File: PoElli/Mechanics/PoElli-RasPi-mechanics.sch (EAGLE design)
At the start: 30 parts, among them J1 DF12-ELLI-HEADER-TOP, J3 M022.54MM, J4 M022.54MM, T1 Coilcraft 230NL, T2 FLYBACK750311689, U3 FST3257, X1 M-BOLT-2, X2 M-BOLT-2, X3 M-BOLT-2, X4 M-BOLT-2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

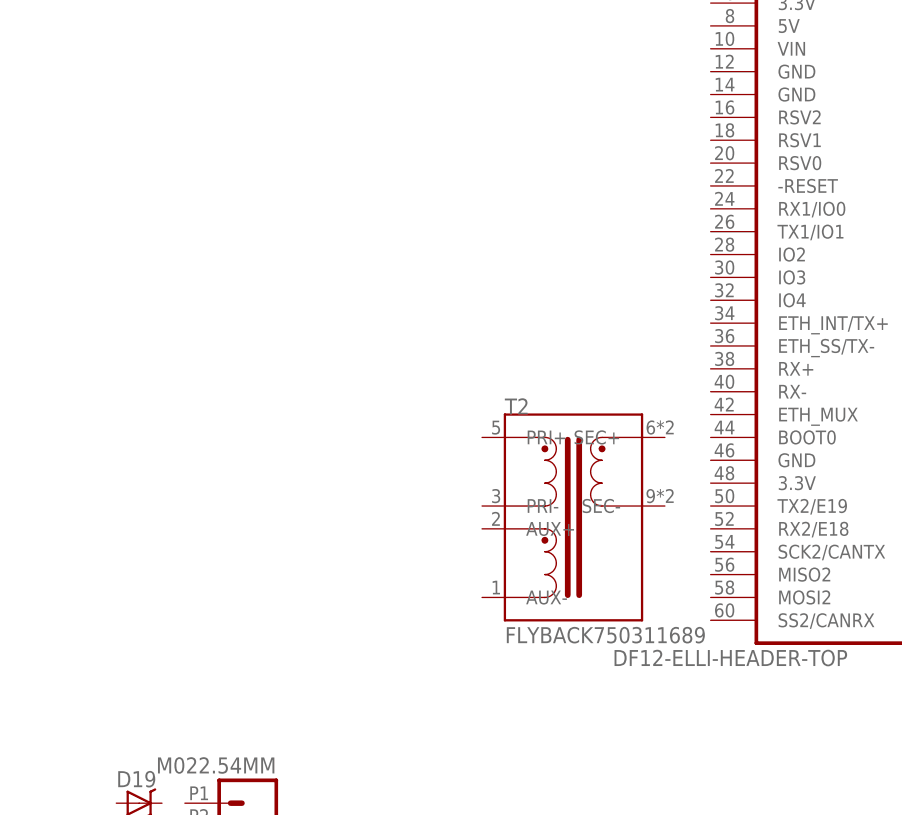
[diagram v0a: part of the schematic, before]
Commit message: Update PoElli/Mechanics non-produced boards with new library components
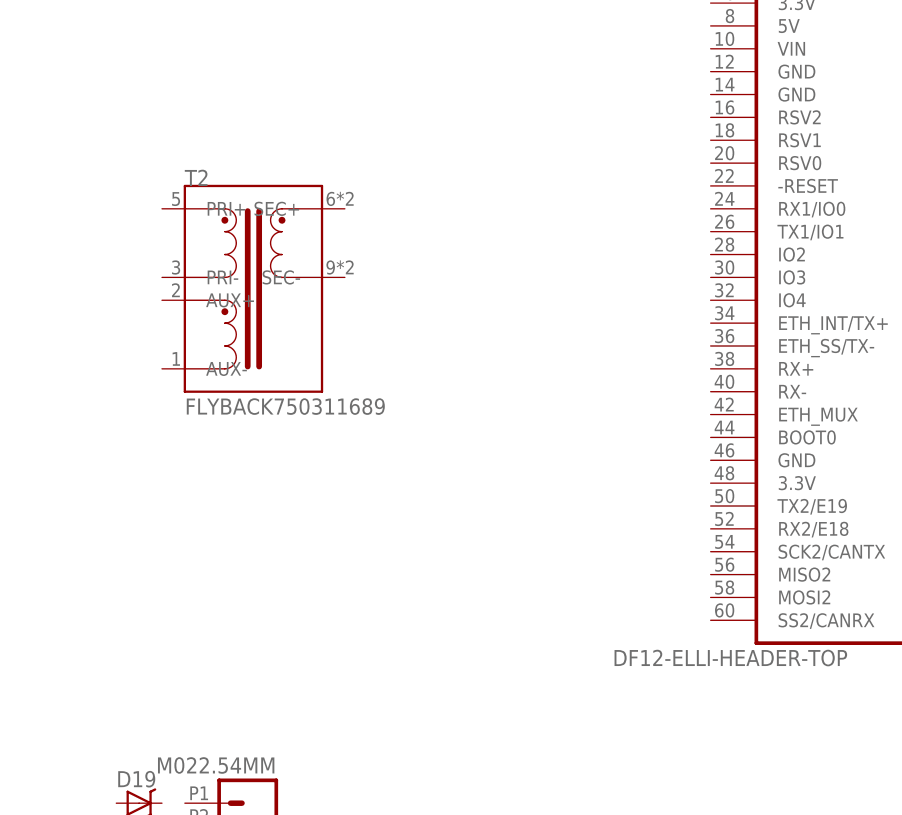
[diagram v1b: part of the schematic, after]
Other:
- moved on the sheet: T2
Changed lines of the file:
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@@
 <grid distance="0.1" unitdist="inch" unit="inch" style="lines" multiple="1" display="no" altdistance="0.01" altunitdist="inch" altunit="inch"/>
 <layers>
-<layer number="1" name="Top" color="4" fill="1" visible="yes" active="no"/>
-<layer number="16" name="Bottom" color="1" fill="1" visible="yes" active="no"/>
-<layer number="17" name="Pads" color="2" fill="1" visible="yes" active="no"/>
-<layer number="18" name="Vias" color="2" fill="1" visible="yes" active="no"/>
-<layer number="19" name="Unrouted" color="6" fill="1" visible="yes" active="no"/>
-<layer number="20" name="Dimension" color="15" fill="1" visible="yes" active="no"/>
-<layer number="21" name="tPlace" color="7" fill="1" visible="yes" active="no"/>
-<layer number="22" name="bPlace" color="7" fill="1" visible="yes" active="no"/>
-<layer number="23" name="tOrigins" color="15" fill="1" visible="yes" active="no"/>
-<layer number="24" name="bOrigins" color="15" fill="1" visible="yes" active="no"/>
-<layer number="25" name="tNames" color="7" fill="1" visible="yes" active="no"/>
-<layer number="26" name="bNames" color="7" fill="1" visible="yes" active="no"/>
-<layer number="27" name="tValues" color="7" fill="1" visible="yes" active="no"/>
-<layer number="28" name="bValues" color="7" fill="1" visible="yes" active="no"/>
+<layer number="1" name="Top" color="4" fill="1" visible="no" active="no"/>
+<layer number="16" name="Bottom" color="1" fill="1" visible="no" active="no"/>
+<layer number="17" name="Pads" color="2" fill="1" visible="no" active="no"/>
+<layer number="18" name="Vias" color="2" fill="1" visible="no" active="no"/>
+<layer number="19" name="Unrouted" color="6" fill="1" visible="no" active="no"/>
+<layer number="20" name="Dimension" color="15" fill="1" visible="no" active="no"/>
+<layer number="21" name="tPlace" color="7" fill="1" visible="no" active="no"/>
+<layer number="22" name="bPlace" color="7" fill="1" visible="no" active="no"/>
+<layer number="23" name="tOrigins" color="15" fill="1" visible="no" active="no"/>
+<layer number="24" name="bOrigins" color="15" fill="1" visible="no" active="no"/>
+<layer number="25" name="tNames" color="7" fill="1" visible="no" active="no"/>
+<layer number="26" name="bNames" color="7" fill="1" visible="no" active="no"/>
+<layer number="27" name="tValues" color="7" fill="1" visible="no" active="no"/>
+<layer number="28" name="bValues" color="7" fill="1" visible="no" active="no"/>
 <layer number="29" name="tStop" color="7" fill="3" visible="no" active="no"/>
 <layer number="30" name="bStop" color="7" fill="6" visible="no" active="no"/>
@@
 <layer number="35" name="tGlue" color="7" fill="4" visible="no" active="no"/>
 <layer number="36" name="bGlue" color="7" fill="5" visible="no" active="no"/>
-<layer number="37" name="tTest" color="7" fill="1" visible="yes" active="no"/>
-<layer number="38" name="bTest" color="7" fill="1" visible="yes" active="no"/>
+<layer number="37" name="tTest" color="7" fill="1" visible="no" active="no"/>
+<layer number="38" name="bTest" color="7" fill="1" visible="no" active="no"/>
 <layer number="39" name="tKeepout" color="4" fill="11" visible="no" active="no"/>
 <layer number="40" name="bKeepout" color="1" fill="11" visible="no" active="no"/>
@@
 <layer number="44" name="Drills" color="7" fill="1" visible="no" active="no"/>
 <layer number="45" name="Holes" color="7" fill="1" visible="no" active="no"/>
-<layer number="46" name="Milling" color="3" fill="1" visible="yes" active="no"/>
-<layer number="47" name="Measures" color="7" fill="1" visible="yes" active="no"/>
-<layer number="48" name="Document" color="7" fill="1" visible="yes" active="no"/>
-<layer number="49" name="Reference" color="7" fill="1" visible="yes" active="no"/>
-<layer number="50" name="dxf" color="7" fill="1" visible="yes" active="no"/>
-<layer number="51" name="tDocu" color="7" fill="1" visible="yes" active="no"/>
-<layer number="52" name="bDocu" color="7" fill="1" visible="yes" active="no"/>
-<layer number="53" name="tGND_GNDA" color="7" fill="9" visible="yes" active="no"/>
-<layer number="54" name="bGND_GNDA" color="1" fill="9" visible="yes" active="no"/>
-<layer number="56" name="wert" color="7" fill="1" visible="yes" active="no"/>
-<layer number="57" name="tCopper" color="7" fill="1" visible="yes" active="no"/>
-<layer number="58" name="bCopper" color="7" fill="1" visible="yes" active="no"/>
+<layer number="46" name="Milling" color="3" fill="1" visible="no" active="no"/>
+<layer number="47" name="Measures" color="7" fill="1" visible="no" active="no"/>
+<layer number="48" name="Document" color="7" fill="1" visible="no" active="no"/>
+<layer number="49" name="Reference" color="7" fill="1" visible="no" active="no"/>
+<layer number="50" name="dxf" color="7" fill="1" visible="no" active="no"/>
+<layer number="51" name="tDocu" color="7" fill="1" visible="no" active="no"/>
+<layer number="52" name="bDocu" color="7" fill="1" visible="no" active="no"/>
+<layer number="53" name="tGND_GNDA" color="7" fill="9" visible="no" active="no"/>
+<layer number="54" name="bGND_GNDA" color="1" fill="9" visible="no" active="no"/>
+<layer number="56" name="wert" color="7" fill="1" visible="no" active="no"/>
+<layer number="57" name="tCopper" color="7" fill="1" visible="no" active="no"/>
+<layer number="58" name="bCopper" color="7" fill="1" visible="no" active="no"/>
 <layer number="91" name="Nets" color="2" fill="1" visible="yes" active="yes"/>
 <layer number="92" name="Busses" color="1" fill="1" visible="yes" active="yes"/>
@@
 <instance part="D8" gate="G$1" x="38.1" y="88.9" rot="R90"/>
 <instance part="D7" gate="G$1" x="33.02" y="88.9" rot="R90"/>
-<instance part="T2" gate="G$1" x="205.74" y="43.18"/>
+<instance part="T2" gate="G$1" x="170.18" y="68.58"/>
 <instance part="J4" gate="G$1" x="7.62" y="7.62"/>
 <instance part="U3" gate="G$1" x="147.32" y="152.4"/>

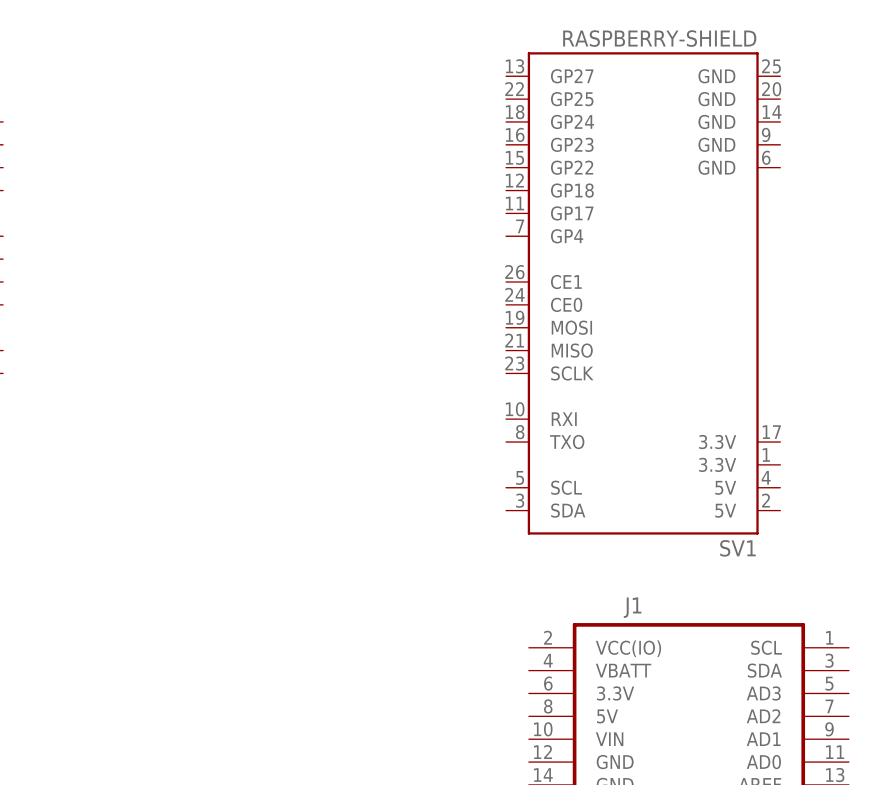
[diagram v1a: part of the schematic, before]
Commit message: Update RasPi outline & connector
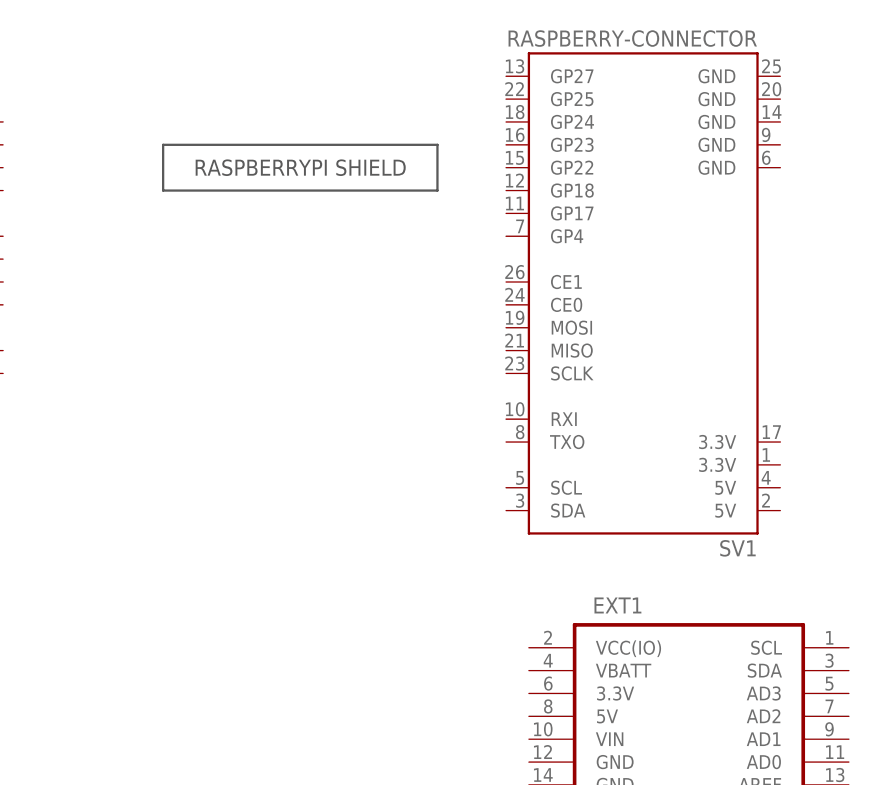
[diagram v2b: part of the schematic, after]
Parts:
- added OUTLINE1: RASPBERRY-OUTLINE, ELL-i-Boards:RASPBERRY-OUTLINE
- SV1: value RASPBERRY-SHIELD -> RASPBERRY-CONNECTOR; device ELL-i-Boards:RASPBERRY-SHIELD -> ELL-i-Boards:RASPBERRY-CONNECTOR
- renumbered J1 to EXT1
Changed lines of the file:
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@@
 <layer number="111" name="111" color="7" fill="1" visible="yes" active="yes"/>
 <layer number="112" name="tSilk" color="7" fill="1" visible="yes" active="yes"/>
+<layer number="113" name="IDFDebug" color="4" fill="1" visible="yes" active="yes"/>
 <layer number="116" name="Patch_BOT" color="9" fill="4" visible="yes" active="yes"/>
 <layer number="118" name="Rect_Pads" color="7" fill="1" visible="yes" active="yes"/>
@@
 <parts>
 <part name="T1" library="ELL-i-Transformers" deviceset="POE-ISOLATION" device="-230NL" value="Coilcraft 230NL"/>
-<part name="SV1" library="ELL-i-Boards" deviceset="RASPBERRY-SHIELD" device=""/>
-<part name="J1" library="ELL-i-Connectors" deviceset="DF12-ELLI-*" device="HEADER-TOP"/>
+<part name="SV1" library="ELL-i-Boards" deviceset="RASPBERRY-CONNECTOR" device=""/>
+<part name="EXT1" library="ELL-i-Connectors" deviceset="DF12-ELLI-*" device="HEADER-TOP"/>
 <part name="D17" library="ELL-i-DIscreteSemi" deviceset="DIODE-SCHOTTKY" device="B2100" value="B2100"/>
 <part name="D16" library="ELL-i-DIscreteSemi" deviceset="DIODE-SCHOTTKY" device="B2100" value="B2100"/>
@@
 <part name="X4" library="ELL-i-Connectors" deviceset="M-BOLT" device="-2"/>
 <part name="X5" library="ELL-i-Connectors" deviceset="POE-TP" device="-RJ45-4UCON" value="POE-TP-RJ45-4UCON"/>
+<part name="OUTLINE1" library="ELL-i-Boards" deviceset="RASPBERRY-OUTLINE" device=""/>
 </parts>
 <sheets>
@@
 <instance part="T1" gate="G$1" x="88.9" y="139.7" rot="R180"/>
 <instance part="SV1" gate="G$1" x="233.68" y="144.78" rot="R180"/>
-<instance part="J1" gate="E" x="238.76" y="68.58" rot="MR0"/>
+<instance part="EXT1" gate="E" x="238.76" y="68.58" rot="MR0"/>
 <instance part="D17" gate="G$1" x="48.26" y="38.1" rot="R90"/>
 <instance part="D16" gate="G$1" x="43.18" y="38.1" rot="R90"/>
@@
 <instance part="X4" gate="M" x="88.138" y="66.04" rot="MR0"/>
 <instance part="X5" gate="G$1" x="35.56" y="144.78" rot="R180"/>
+<instance part="OUTLINE1" gate="G$1" x="195.58" y="157.48"/>
 </instances>
 <busses>
@@
 <net name="RTN" class="0">
 <segment>
-<pinref part="SUPPLY9" gate="G$1" pin="RTN"/>
+<pinref part="SUPPLY9" gate="G$1" pin="SGND"/>
 <wire x1="33.02" y1="121.92" x2="33.02" y2="127" width="0.1524" layer="91"/>
 <wire x1="33.02" y1="127" x2="33.02" y2="129.54" width="0.1524" layer="91"/>
